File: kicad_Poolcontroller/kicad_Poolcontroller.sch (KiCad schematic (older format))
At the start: 56 parts, among them J1 Conn_02x01, J10 Conn_01x04, J11 Conn_01x04, J12 Conn_01x04, J13 Conn_01x04, J2 Conn_02x02_Odd_Even, J3 Conn_02x02_Odd_Even, J4 Conn_01x04, J5 ESP01, J6 Conn_01x04, J7 Conn_01x04, J8 Conn_01x04, J9 Conn_01x04, K1 SANYOU_SRD_Form_C, K2 SANYOU_SRD_Form_C, K3 SANYOU_SRD_Form_C, K4 SANYOU_SRD_Form_C, K5 SANYOU_SRD_Form_C, K6 SANYOU_SRD_Form_C, K7 SANYOU_SRD_Form_C, K8 SANYOU_SRD_Form_C, Q1 2N2219, Q2 2N2219, Q3 2N2219, Q4 2N2219, Q5 2N2219, Q6 2N2219, Q7 2N2219, Q8 2N2219, U1 ATtiny85V-10PU, U2 74HC595, U3 L7809, U4 L7805, U5 LM317

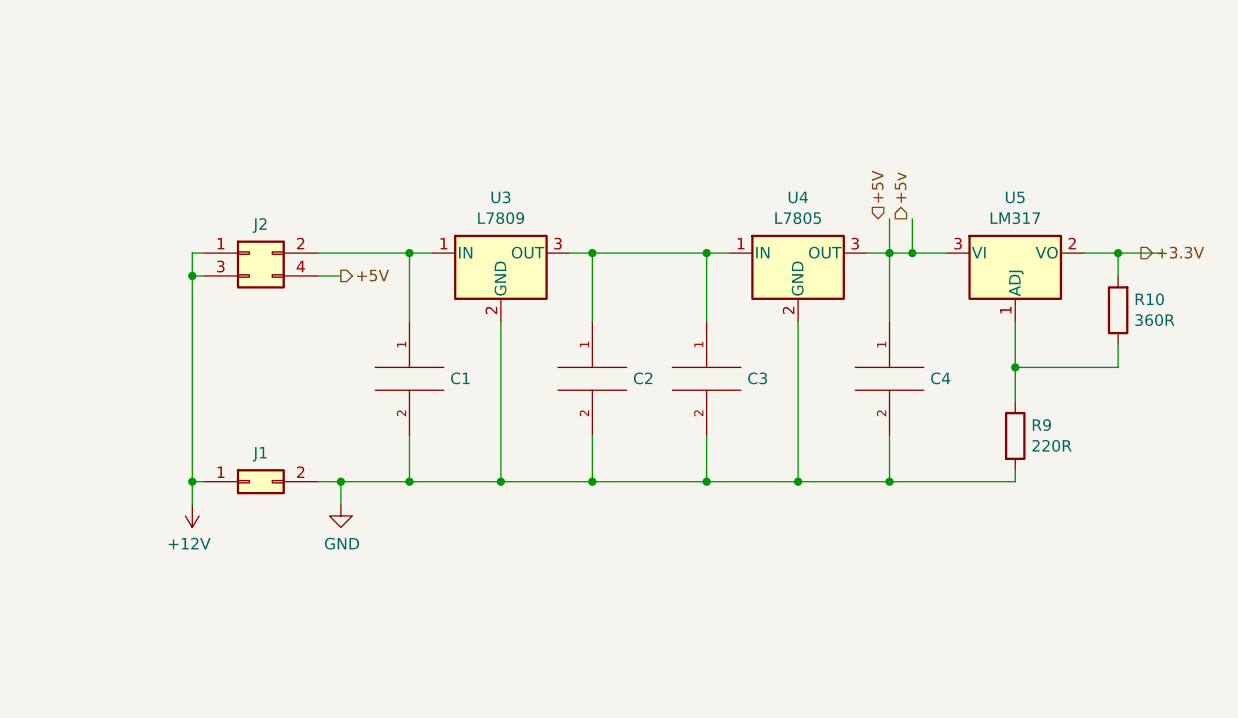
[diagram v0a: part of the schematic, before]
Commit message: 1.01
retirada da possibilidade de alimentar a placa inteira com 12V
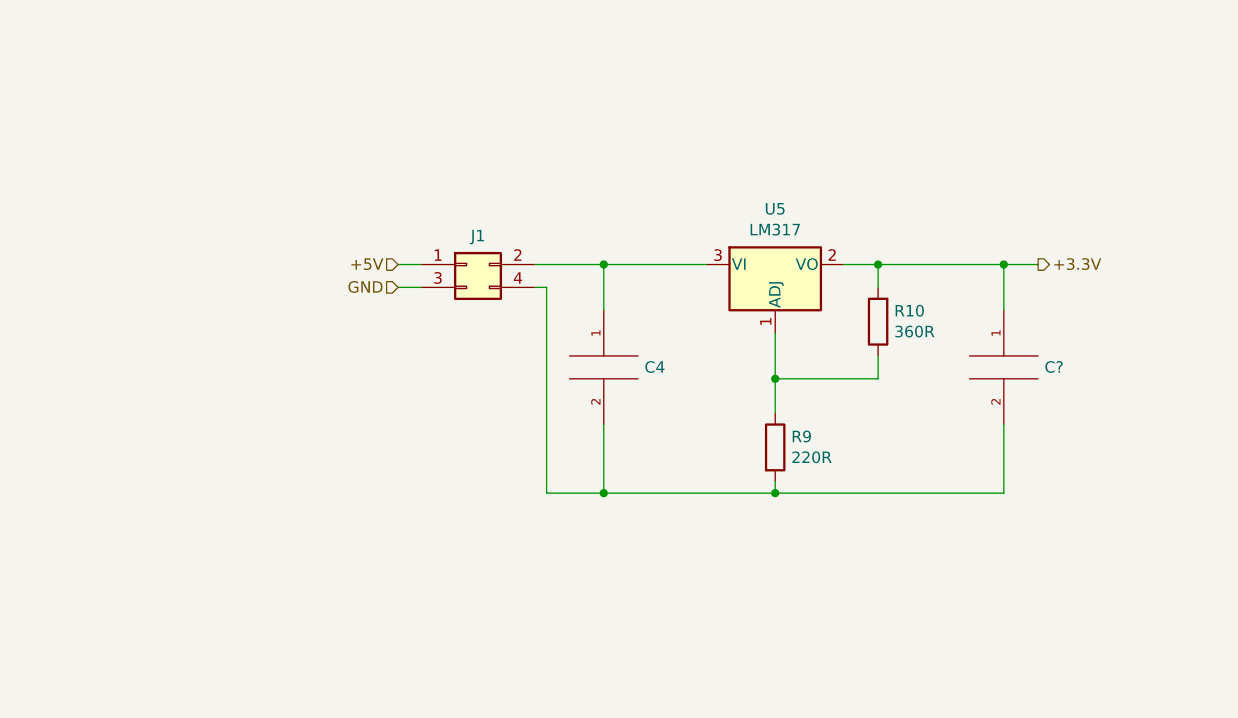
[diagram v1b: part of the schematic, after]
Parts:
- removed C1, C3: 220u, Capacitor_THT:CP_Radial_D5.0mm_P2.50mm, symbol pspice:C
- removed C2: 47u, Capacitor_THT:CP_Radial_D5.0mm_P2.50mm, symbol pspice:C
- removed J1: Conn_02x01, Connector_PinHeader_2.54mm:PinHeader_2x01_P2.54mm_Vertical, symbol Connector_Generic:Conn_02x01
- removed J2: Conn_02x02_Odd_Even, Connector_PinHeader_2.54mm:PinHeader_2x02_P2.54mm_Vertical, symbol Connector_Generic:Conn_02x02_Odd_Even
- removed U3: L7809, Package_TO_SOT_THT:TO-220-3_Vertical, symbol Regulator_Linear:L7809
- removed U4: L7805, Package_TO_SOT_THT:TO-220-3_Vertical, symbol Regulator_Linear:L7805
- added C?: 10u, Capacitor_THT:CP_Radial_D5.0mm_P2.50mm, symbol pspice:C
- added J1: Conn_02x02_Odd_Even, symbol Connector_Generic:Conn_02x02_Odd_Even
- C4: value 47u -> 0.1u
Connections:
- net +3.3V: now also C?.1
- net +5V: now also J1.1 (Pin_1)
- net GND: now also J1.3 (Pin_3); no longer C4.2, R9.2
- net at C4.1, U5.3 (VI): now also J1.2 (Pin_2)
- new net: C4.2, C?.2, J1.4 (Pin_4), R9.2
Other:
- moved on the sheet: C4, R10, R9, U5

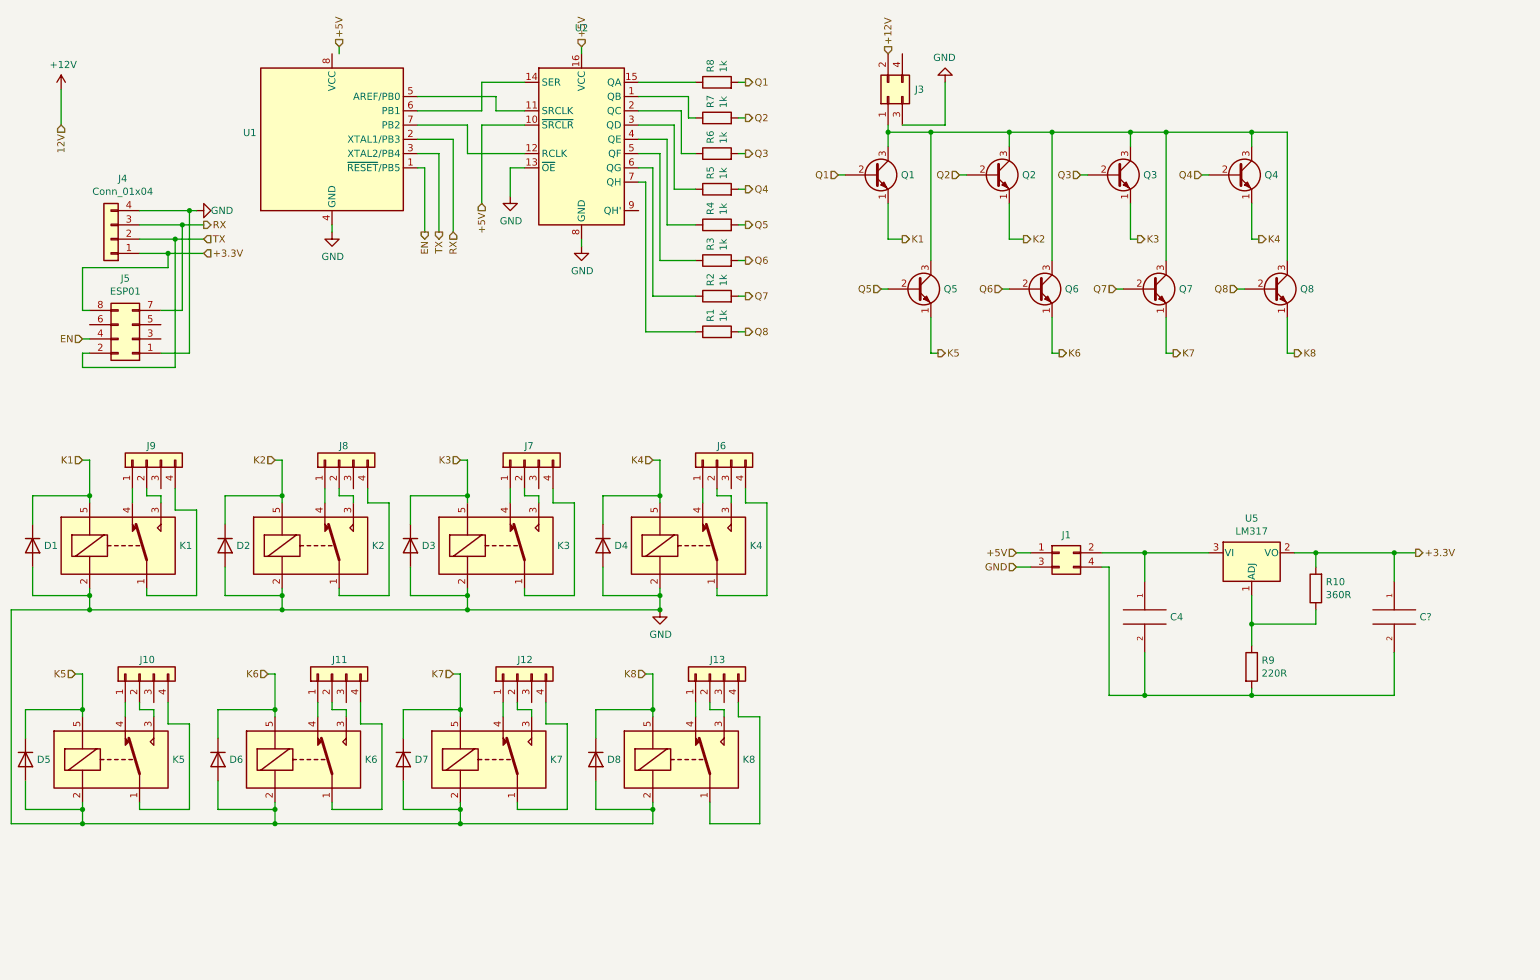
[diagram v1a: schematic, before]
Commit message: 1.0.2
adicionado o divisor de tensão para o TX dos módulos de comunicação
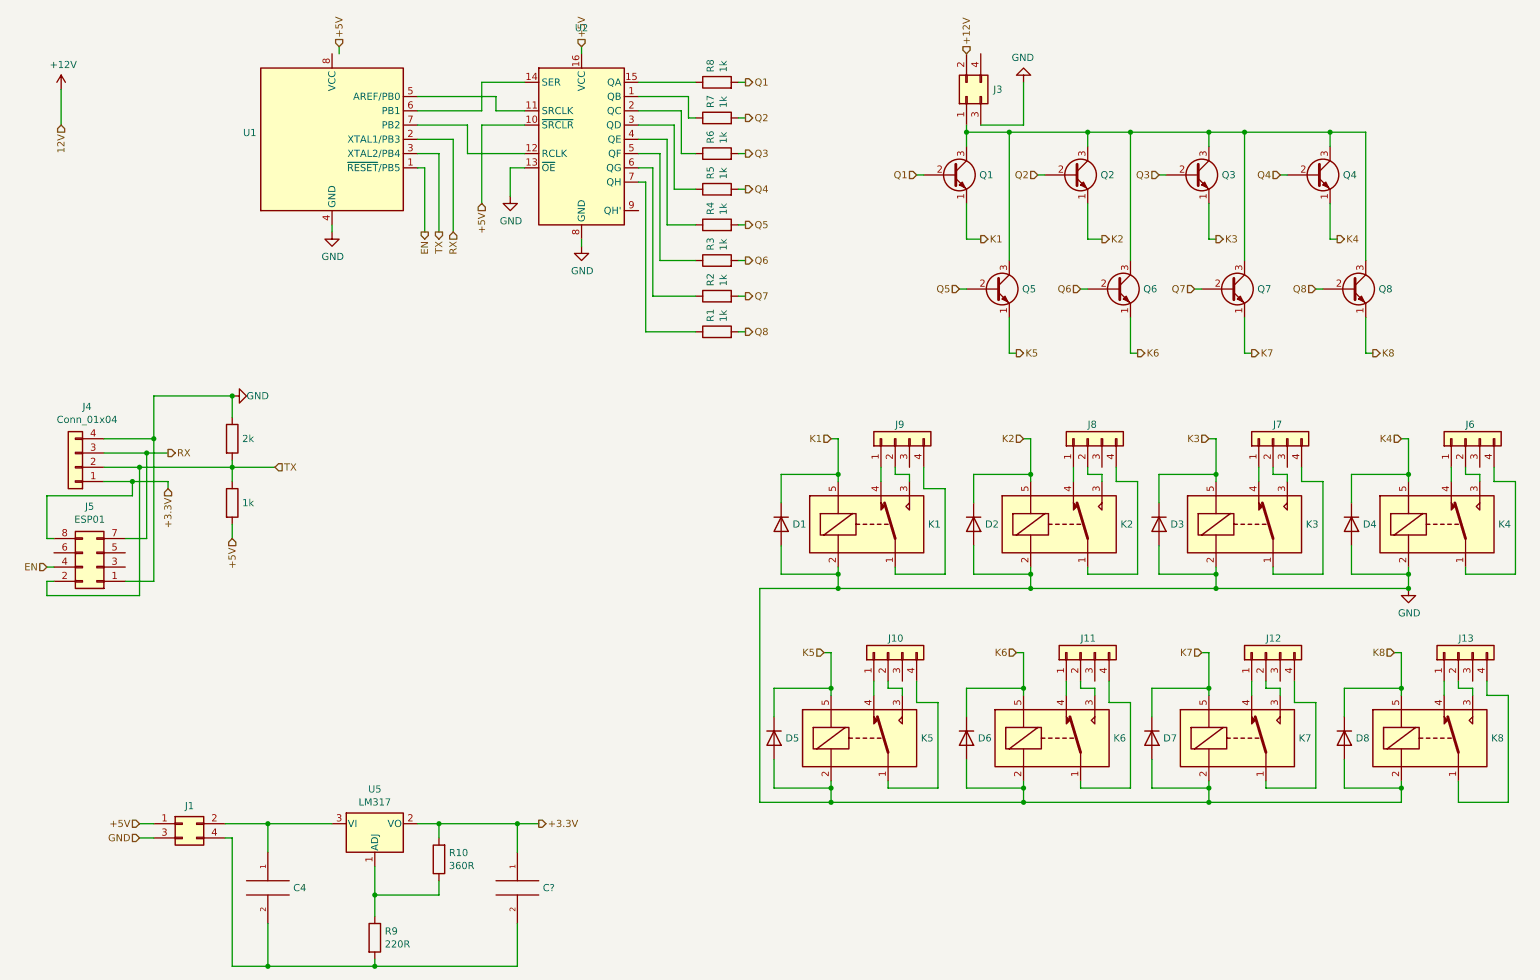
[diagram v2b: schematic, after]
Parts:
- added R?: 2k, symbol Device:R
- added R?: 1k, symbol Device:R
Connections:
- net +5V: now also R?.2
- net GND: now also R?.1
- net TX: now also R?.1, R?.2
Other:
- moved on the sheet: C4, C?, D1, D2, D3, D4, D5, D6, D7, D8, J1, J10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

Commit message: att
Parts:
- removed J3: Conn_02x02_Odd_Even, Connector_PinHeader_2.54mm:PinHeader_2x02_P2.54mm_Vertical, symbol Connector_Generic:Conn_02x02_Odd_Even
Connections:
- net +5V: now also Q1.3 (C), Q2.3 (C), Q3.3 (C), Q4.3 (C), Q5.3 (C), Q6.3 (C), Q7.3 (C), Q8.3 (C)
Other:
- moved on the sheet: C4, C?, D1, D2, D3, D4, D5, D6, D7, D8, J1, J10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
